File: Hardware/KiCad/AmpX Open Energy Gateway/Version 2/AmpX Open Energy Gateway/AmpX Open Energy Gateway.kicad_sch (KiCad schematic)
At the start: 15 parts, among them J1 POW, J2 STATUS, J3 Status Conn Top, U2 W5500, U3 ESP32-DEVKITC-32U

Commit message: Micheal changes
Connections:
- net DE: no longer names the net of U3.26 (IO4)
- net RX: no longer names the net of U3.27 (IO16)
- net TX: no longer names the net of U3.28 (IO17)

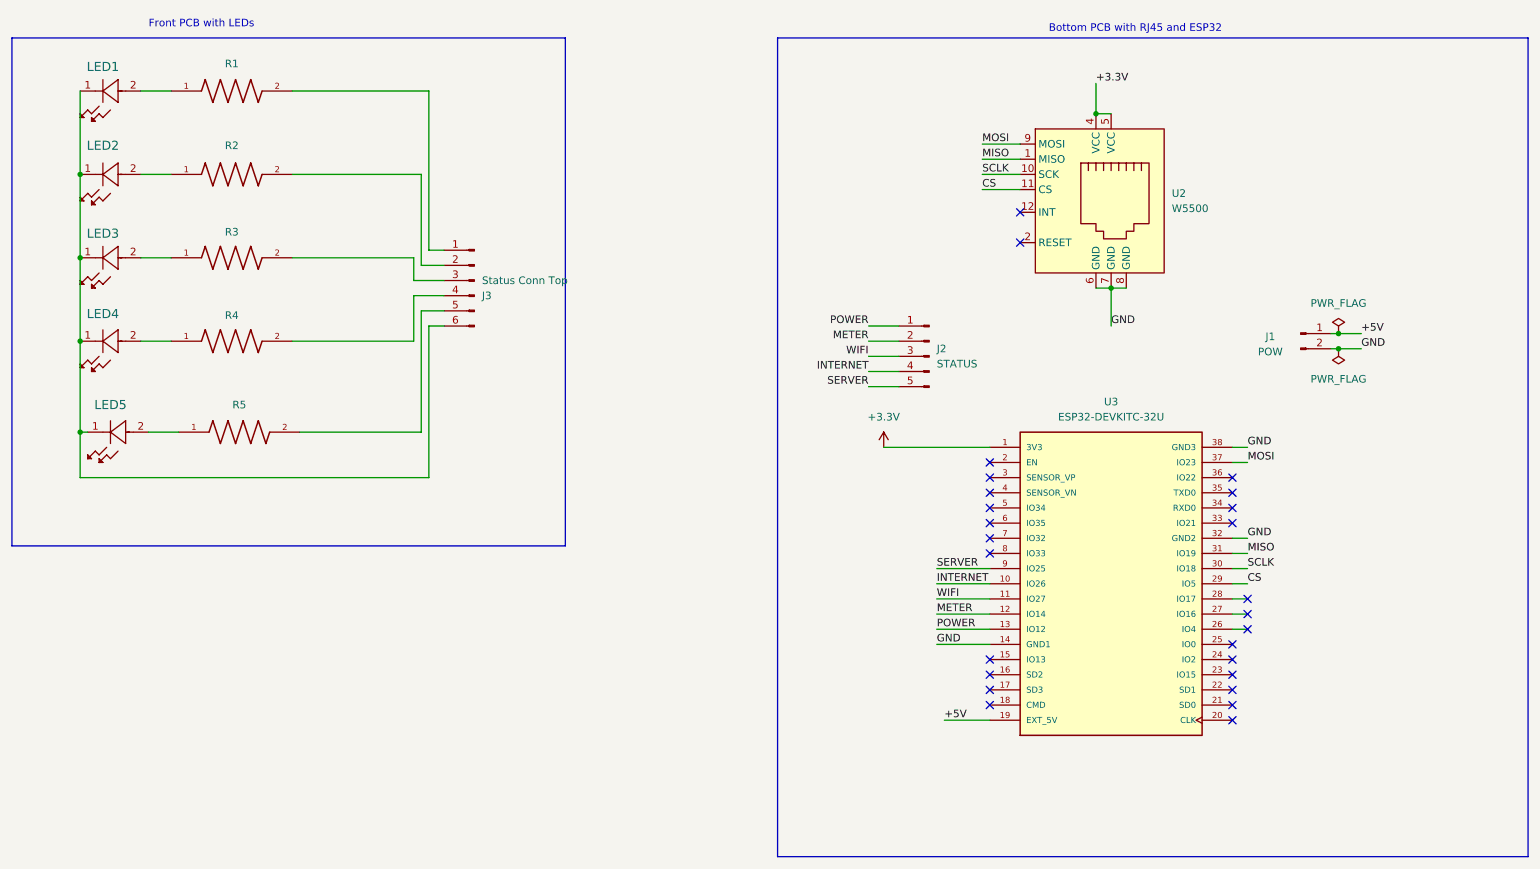
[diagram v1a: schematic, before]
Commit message: feat: separate front and bottom pcbs
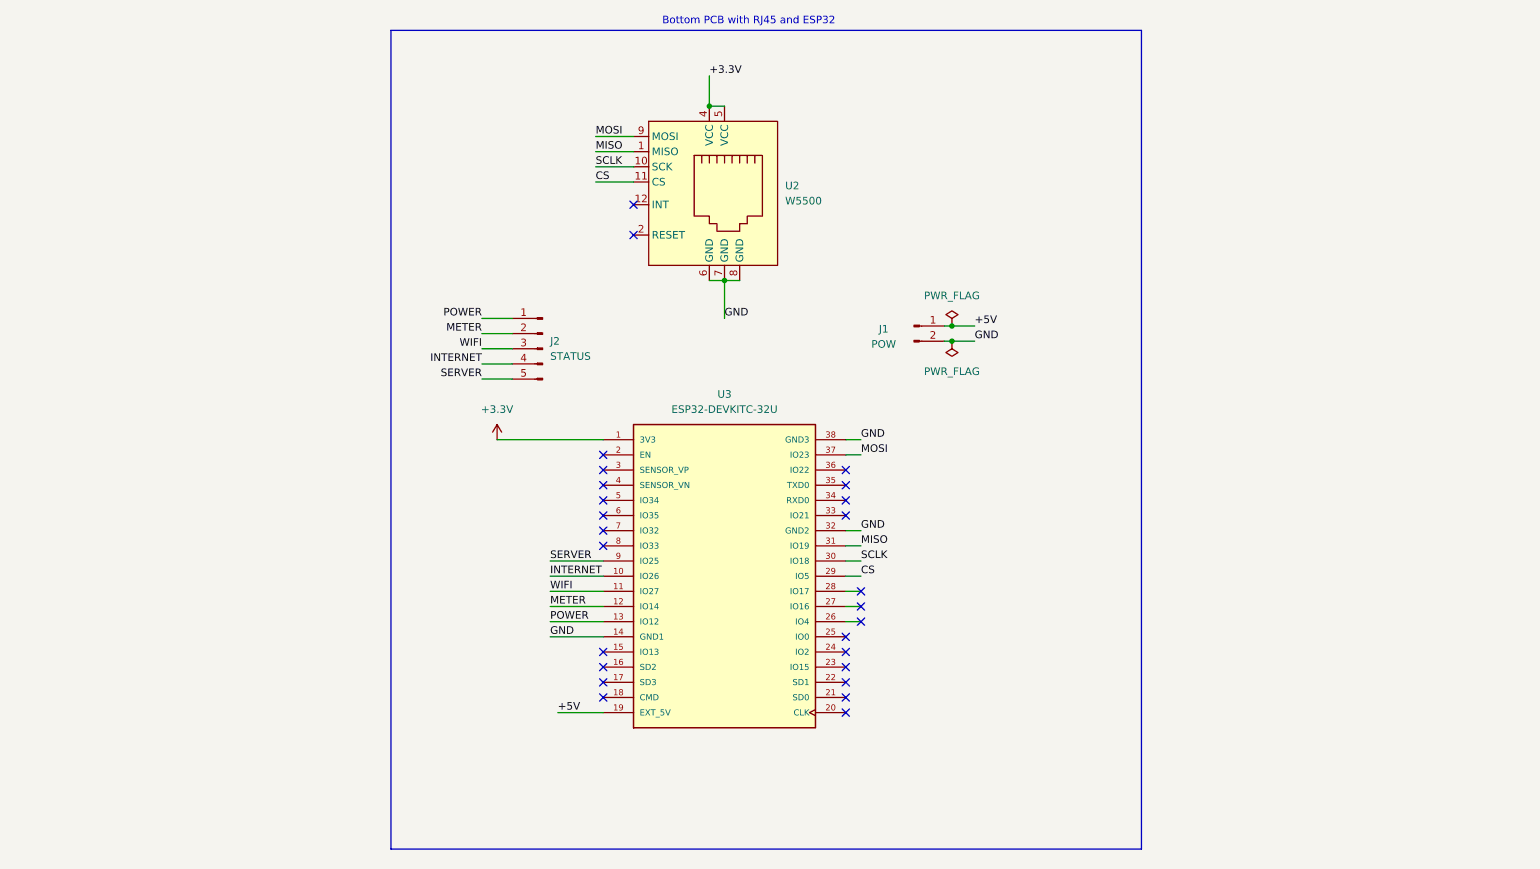
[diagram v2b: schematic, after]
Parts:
- removed J3: Status Conn Top, Connector_Wire:SolderWire-0.5sqmm_1x06_P4.6mm_D0.9mm_OD2.1mm, symbol Connector:Conn_01x06_Pin
- removed LED1, LED2, LED3, LED4, LED5: CMD15-21VGD/TR8, AmpX-Footprint-Library.pretty:LED_GREEN_CMD15-21_VCC, symbol AmpX_Library_1:LED_GREEN_CMD15-21VGD_TR8
- removed R1, R2, R3, R4, R5: Resistor SMD DigiKey ERJ-T06J221V, AmpX-Footprint-Library.pretty:Resistor_SMD_Digikey_RESC2012X70N, symbol AmpX_Library_1:Resistor SMD DigiKey ERJ-T06J221V
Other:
- note removed: "Front PCB with LEDs"
- moved on the sheet: J1, J2, U2, U3

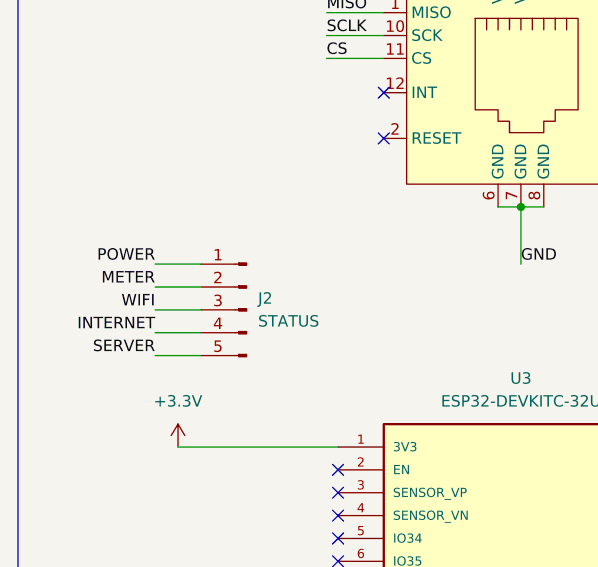
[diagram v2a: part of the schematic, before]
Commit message: added extra wire for ground
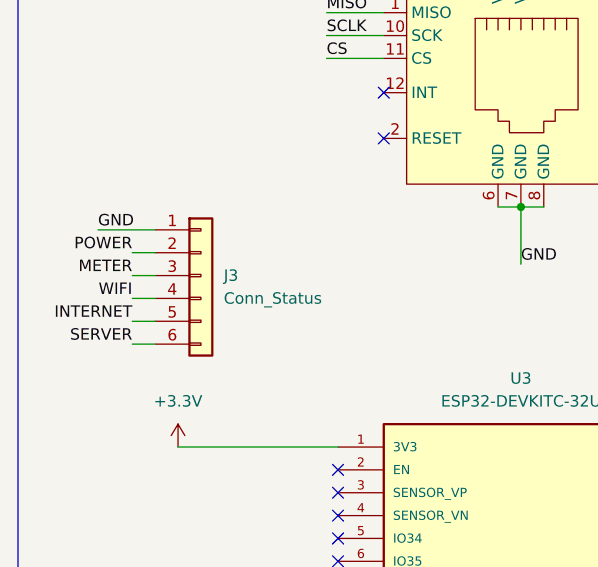
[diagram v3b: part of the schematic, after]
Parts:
- removed J2: STATUS, Connector_JST:JST_XH_B5B-XH-A_1x05_P2.50mm_Vertical, symbol Connector:Conn_01x05_Pin
- added J3: Conn_Status, Connector_JST:JST_ZH_B6B-ZR_1x06_P1.50mm_Vertical, symbol Connector_Generic:Conn_01x06
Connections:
- net GND: now also J3.1 (Pin_1)
- net INTERNET: now also J3.5 (Pin_5)
- net METER: now also J3.3 (Pin_3)
- net POWER: now also J3.2 (Pin_2)
- net SERVER: now also J3.6 (Pin_6)
- net WIFI: now also J3.4 (Pin_4)
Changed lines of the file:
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@@
-	(wire
-		(pts
-			(xy 99.06 74.93) (xy 104.14 74.93)
-		)
-		(stroke
-			(width 0)
-			(type default)
-		)
-	)
 	(wire
 		(pts
@@
 	(wire
 		(pts
-			(xy 99.06 80.01) (xy 104.14 80.01)
-		)
-		(stroke
-			(width 0)
-			(type default)
-		)
-	)
-	(wire
-		(pts
 			(xy 111.76 138.43) (xy 119.38 138.43)
 		)
@@
 	(wire
 		(pts
-			(xy 99.06 77.47) (xy 104.14 77.47)
-		)
-		(stroke
-			(width 0)
-			(type default)
-		)
-	)
-	(wire
-		(pts
 			(xy 139.7 66.04) (xy 142.24 66.04)
 		)
@@
 	(wire
 		(pts
+			(xy 96.52 81.28) (xy 99.06 81.28)
+		)
+		(stroke
+			(width 0)
+			(type default)
+		)
+	)
+	(wire
+		(pts
+			(xy 96.52 73.66) (xy 99.06 73.66)
+		)
+		(stroke
+			(width 0)
+			(type default)
+		)
+	)
+	(wire
+		(pts
 			(xy 177.8 73.66) (xy 176.53 73.66)
 		)
@@
 	(wire
 		(pts
-			(xy 104.14 72.39) (xy 99.06 72.39)
+			(xy 96.52 71.12) (xy 99.06 71.12)
+		)
+		(stroke
+			(width 0)
+			(type default)
+		)
+	)
+	(wire
+		(pts
+			(xy 92.71 68.58) (xy 99.06 68.58)
 		)
 		(stroke
@@
 	(wire
 		(pts
+			(xy 96.52 76.2) (xy 99.06 76.2)
+		)
+		(stroke
+			(width 0)
+			(type default)
+		)
+	)
+	(wire
+		(pts
 			(xy 137.16 36.83) (xy 139.7 36.83)
 		)
@@
 	(wire
 		(pts
-			(xy 99.06 82.55) (xy 104.14 82.55)
-		)
-		(stroke
-			(width 0)
-			(type default)
-		)
-	)
-	(label "WIFI"
-		(at 99.06 77.47 180)
+			(xy 96.52 78.74) (xy 99.06 78.74)
+		)
+		(stroke
+			(width 0)
+			(type default)
+		)
+	)
+	(label "POWER"
+		(at 96.52 71.12 180)
 		(effects
 			(font
@@
 		)
 	)
-	(label "SERVER"
-		(at 99.06 82.55 180)
-		(effects
-			(font
-				(size 1.27 1.27)
-			)
-			(justify right bottom)
+	(label "GND"
+		(at 92.71 68.58 0)
+		(effects
+			(font
+				(size 1.27 1.27)
+			)
+			(justify left bottom)
 		)
 	)
@@
 	)
 	(label "POWER"
-		(at 99.06 72.39 180)
+		(at 110.49 123.19 0)
+		(effects
+			(font
+				(size 1.27 1.27)
+			)
+			(justify left bottom)
+		)
+	)
+	(label "SERVER"
+		(at 96.52 81.28 180)
 		(effects
 			(font
@@
 			)
 			(justify right bottom)
-		)
-	)
-	(label "POWER"
-		(at 110.49 123.19 0)
-		(effects
-			(font
-				(size 1.27 1.27)
-			)
-			(justify left bottom)
 		)
 	)
@@
 		)
 	)
-	(label "METER"
-		(at 99.06 74.93 180)
-		(effects
-			(font
-				(size 1.27 1.27)
-			)
-			(justify right bottom)
-		)
-	)
 	(label "SCLK"
 		(at 118.11 46.99 0)
@@
 		)
 	)
-	(label "INTERNET"
-		(at 99.06 80.01 180)
-		(effects
-			(font
-				(size 1.27 1.27)
-			)
-			(justify right bottom)
-		)
-	)
 	(label "GND"
 		(at 162.56 92.71 0)
@@
 		)
 	)
+	(label "METER"
+		(at 96.52 73.66 180)
+		(effects
+			(font
+				(size 1.27 1.27)
+			)
+			(justify right bottom)
+		)
+	)
 	(label "MOSI"
 		(at 118.11 41.91 0)
@@
 		)
 	)
+	(label "INTERNET"
+		(at 96.52 78.74 180)
+		(effects
+			(font
+				(size 1.27 1.27)
+			)
+			(justify right bottom)
+		)
+	)
 	(label "+5V"
 		(at 111.76 138.43 0)
@@
 			)
 			(justify left bottom)
+		)
+	)
+	(label "WIFI"
+		(at 96.52 76.2 180)
+		(effects
+			(font
+				(size 1.27 1.27)
+			)
+			(justify right bottom)
 		)
 	)
@@
 	)
 	(symbol
-		(lib_id "Connector:Conn_01x05_Pin")
-		(at 109.22 77.47 0)
-		(mirror y)
-		(unit 1)
-		(exclude_from_sim no)
-		(in_bom yes)
-		(on_board yes)
-		(dnp no)
-		(fields_autoplaced yes)
-		(property "Reference" "J2"
-			(at 110.49 76.1999 0)
-			(effects
-				(font
-					(size 1.27 1.27)
-				)
-				(justify right)
-			)
-		)
-		(property "Value" "STATUS"
-			(at 110.49 78.7399 0)
-			(effects
-				(font
-					(size 1.27 1.27)
-				)
-				(justify right)
-			)
-		)
-		(property "Footprint" "Connector_JST:JST_XH_B5B-XH-A_1x05_P2.50mm_Vertical"
-			(at 109.22 77.47 0)
-			(effects
-				(font
-					(size 1.27 1.27)
-				)
-				(hide yes)
-			)
-		)
-		(property "Datasheet" "~"
-			(at 109.22 77.47 0)
-			(effects
-				(font
-					(size 1.27 1.27)
-				)
-				(hide yes)
-			)
-		)
-		(property "Description" "Generic connector, single row, 01x05, script generated"
-			(at 109.22 77.47 0)
-			(effects
-				(font
-					(size 1.27 1.27)
-				)
-				(hide yes)
-			)
-		)
-		(pin "5"
-		)
-		(pin "1"
-		)
-		(pin "2"
-		)
-		(pin "3"
-		)
-		(pin "4"
-		)
-		(instances
-			(project ""
-				(path "/548f25e8-745d-4cdd-aa0b-f57ad858b984"
-					(reference "J2")
-					(unit 1)
-				)
-			)
-		)
-	)
-	(symbol
 		(lib_id "power:+3.3V")
 		(at 101.6 92.71 0)
@@
 					(unit 1)
 				)
+			)
+		)
+	)
+	(symbol
+		(lib_id "Connector_Generic:Conn_01x06")
+		(at 104.14 73.66 0)
+		(unit 1)
+		(exclude_from_sim no)
+		(in_bom yes)
+		(on_board yes)
+		(dnp no)
+		(fields_autoplaced yes)
+		(property "Reference" "J3"
+			(at 106.68 73.6599 0)
+			(effects
+				(font
+					(size 1.27 1.27)
+				)
+				(justify left)
+			)
+		)
+		(property "Value" "Conn_Status"
+			(at 106.68 76.1999 0)
+			(effects
+				(font
+					(size 1.27 1.27)
+				)
+				(justify left)
+			)
+		)
+		(property "Footprint" "Connector_JST:JST_ZH_B6B-ZR_1x06_P1.50mm_Vertical"
+			(at 104.14 73.66 0)
+			(effects
+				(font
+					(size 1.27 1.27)
+				)
+				(hide yes)
+			)
+		)
+		(property "Datasheet" "~"
+			(at 104.14 73.66 0)
+			(effects
+				(font
+					(size 1.27 1.27)
+				)
+				(hide yes)
+			)
+		)
+		(property "Description" "Generic connector, single row, 01x06, script generated (kicad-library-utils/schlib/autogen/connector/)"
+			(at 104.14 73.66 0)
+			(effects
+				(font
+					(size 1.27 1.27)
+				)
+				(hide yes)
+			)
+		)
+		(pin "1"
+		)
+		(pin "6"
+		)
+		(pin "3"
+		)
+		(pin "4"
+		)
+		(pin "2"
+		)
+		(pin "5"
+		)
+		(instances
+			(project ""
+				(path "/548f25e8-745d-4cdd-aa0b-f57ad858b984"
+					(reference "J3")
+					(unit 1)
+				)

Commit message: x
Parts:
- J3: footprint Connector_JST:JST_ZH_B6B-ZR_1x06_P1.50mm_Vertical -> Connector_JST:JST_XH_B6B-XH-A_1x06_P2.50mm_Vertical
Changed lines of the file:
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@@
 			)
 		)
-		(property "Footprint" "Connector_JST:JST_ZH_B6B-ZR_1x06_P1.50mm_Vertical"
+		(property "Footprint" "Connector_JST:JST_XH_B6B-XH-A_1x06_P2.50mm_Vertical"
 			(at 104.14 73.66 0)
 			(effects
